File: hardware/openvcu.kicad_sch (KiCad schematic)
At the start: 0 parts

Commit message: Began IGN driver drawings
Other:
- added sheet Ignition Driver (ignition_driver.kicad_sch)
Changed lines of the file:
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@@
 	(paper "A4")
+	(sheet
+		(at 106.045 37.465)
+		(size 25.4 27.94)
+		(exclude_from_sim no)
+		(in_bom yes)
+		(on_board yes)
+		(dnp no)
+		(fields_autoplaced yes)
+		(stroke
+			(width 0.1524)
+			(type solid)
+		)
+		(fill
+			(color 0 0 0 0.0000)
+		)
+		(property "Sheetname" "Ignition Driver"
+			(at 106.045 36.7534 0)
+			(effects
+				(font
+					(size 1.27 1.27)
+				)
+				(justify left bottom)
+			)
+		)
+		(property "Sheetfile" "ignition_driver.kicad_sch"
+			(at 106.045 65.9896 0)
+			(effects
+				(font
+					(size 1.27 1.27)
+				)
+				(justify left top)
+			)
+		)
+		(instances
+			(project "openvcu"
+				(path "/474f8017-6a20-4212-a4d1-1038f3d193b2"
+					(page "3")
+				)
+			)
+		)
+	)
 	(sheet
 		(at 44.45 38.1)

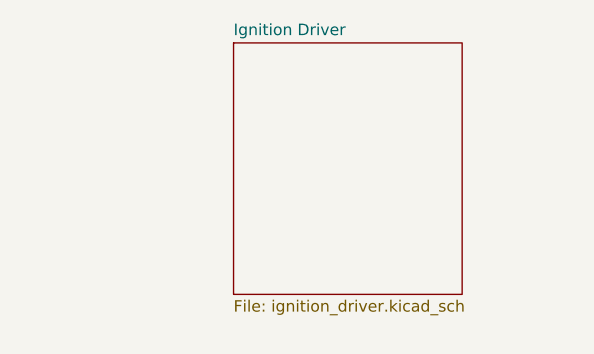
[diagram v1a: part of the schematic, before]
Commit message: Continued IGN driver drawings
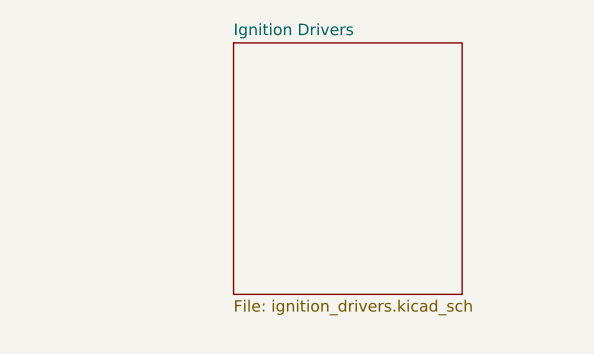
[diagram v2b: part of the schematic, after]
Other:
- sheet Ignition Driver renamed Ignition Drivers
- sheet Ignition Drivers: file ignition_driver.kicad_sch -> ignition_drivers.kicad_sch
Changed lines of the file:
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@@
 			(color 0 0 0 0.0000)
 		)
-		(property "Sheetname" "Ignition Driver"
+		(property "Sheetname" "Ignition Drivers"
 			(at 106.045 36.7534 0)
 			(effects
@@
 			)
 		)
-		(property "Sheetfile" "ignition_driver.kicad_sch"
+		(property "Sheetfile" "ignition_drivers.kicad_sch"
 			(at 106.045 65.9896 0)
 			(effects

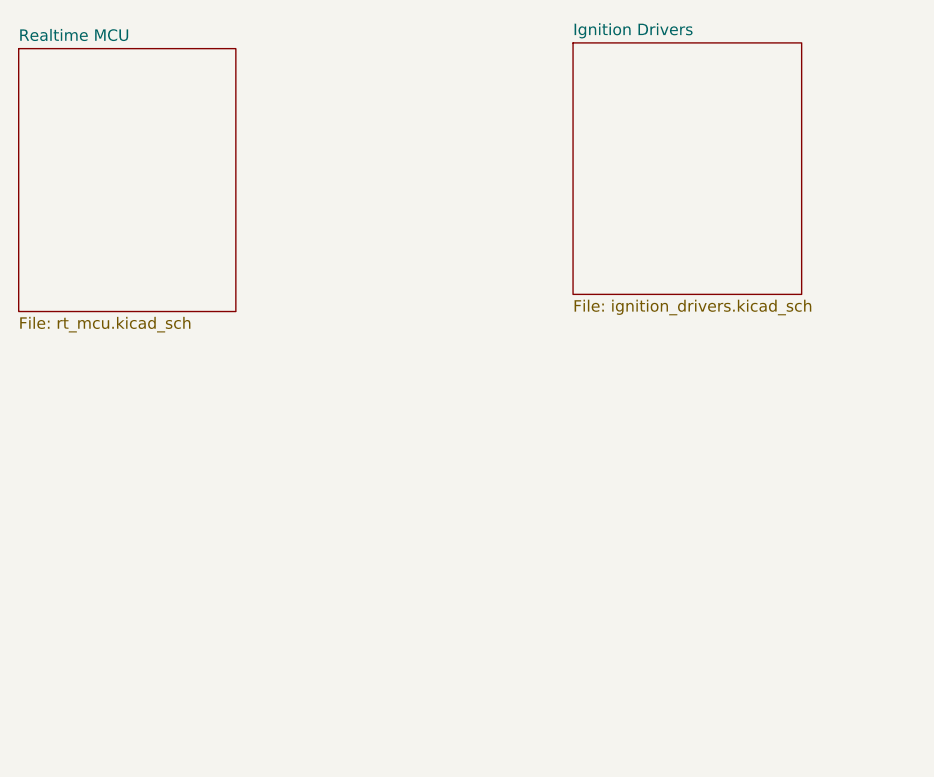
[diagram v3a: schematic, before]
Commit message: Added MOSFET driver symbol
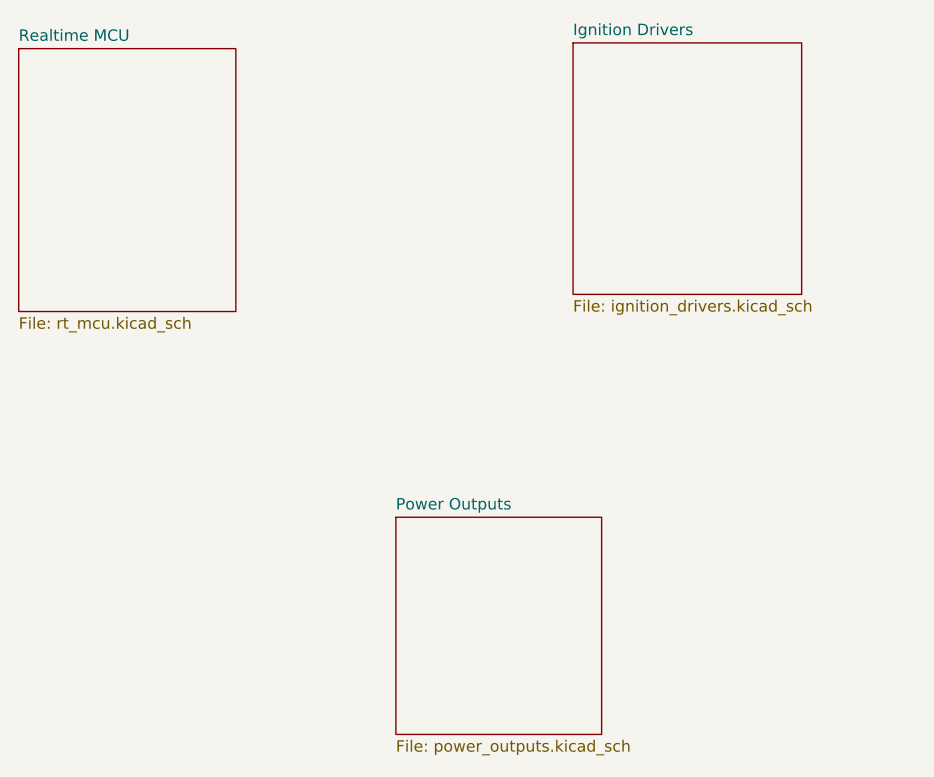
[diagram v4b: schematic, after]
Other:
- added sheet Power Outputs (power_outputs.kicad_sch)
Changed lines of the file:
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@@
 	(paper "A4")
+	(sheet
+		(at 86.36 90.17)
+		(size 22.86 24.13)
+		(exclude_from_sim no)
+		(in_bom yes)
+		(on_board yes)
+		(dnp no)
+		(fields_autoplaced yes)
+		(stroke
+			(width 0.1524)
+			(type solid)
+		)
+		(fill
+			(color 0 0 0 0)
+		)
+		(property "Sheetname" "Power Outputs"
+			(at 86.36 89.4584 0)
+			(show_name no)
+			(do_not_autoplace no)
+			(effects
+				(font
+					(size 1.27 1.27)
+				)
+				(justify left bottom)
+			)
+		)
+		(property "Sheetfile" "power_outputs.kicad_sch"
+			(at 86.36 114.8846 0)
+			(show_name no)
+			(do_not_autoplace no)
+			(effects
+				(font
+					(size 1.27 1.27)
+				)
+				(justify left top)
+			)
+		)
+		(instances
+			(project "openvcu"
+				(path "/474f8017-6a20-4212-a4d1-1038f3d193b2"
+					(page "5")
+				)
+			)
+		)
+	)
 	(sheet
 		(at 106.045 37.465)
